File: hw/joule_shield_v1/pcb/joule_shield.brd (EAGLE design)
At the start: 160 x 100 mm, 65 parts, among them U1 BQ25892PWQFN-24, U2 FAN8623WLCSP16, U3 TPS63201PVSON-14, U4 TLV62084PWSON-8, U5 TPS2553PWSON-6, U6 SINGLE-BIT_BUS_TRANSCEIVER, U7 SINGLE-BIT_BUS_TRANSCEIVER

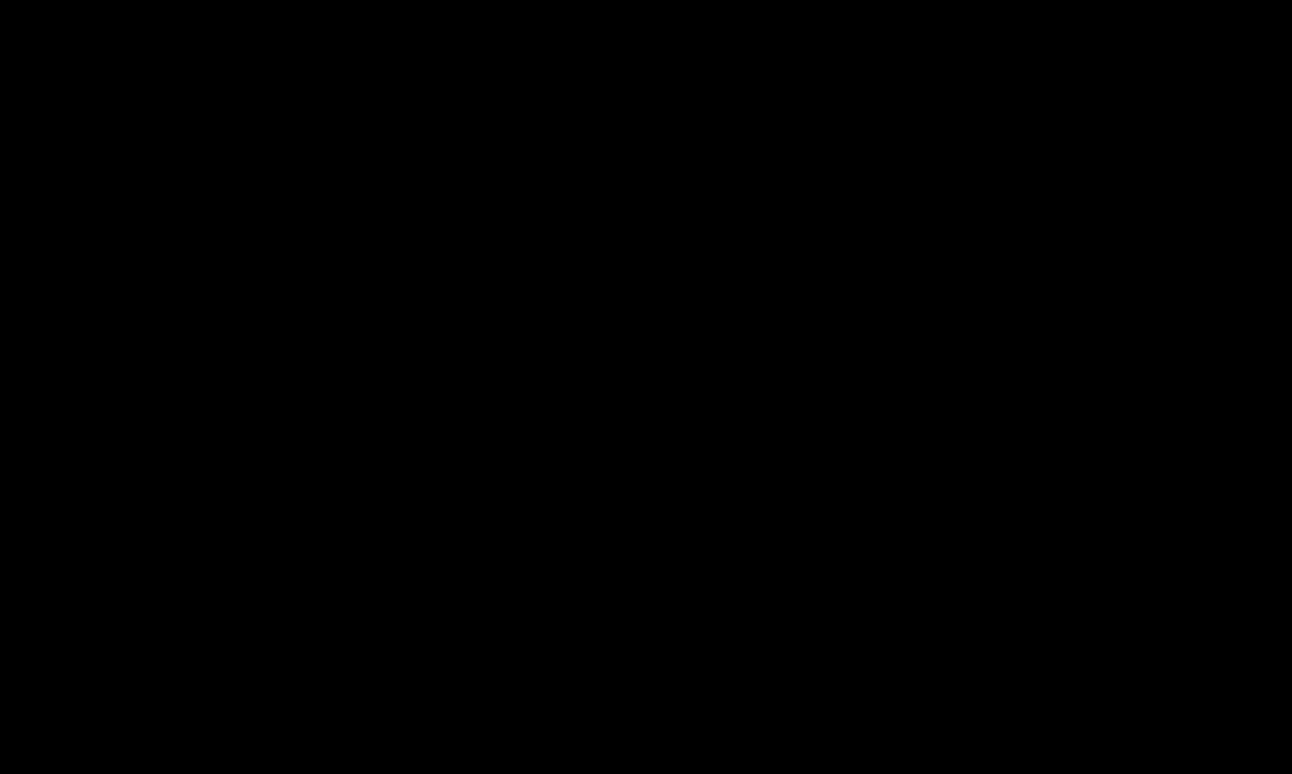
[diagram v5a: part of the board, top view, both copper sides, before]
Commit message: Schematic for servo connectors.
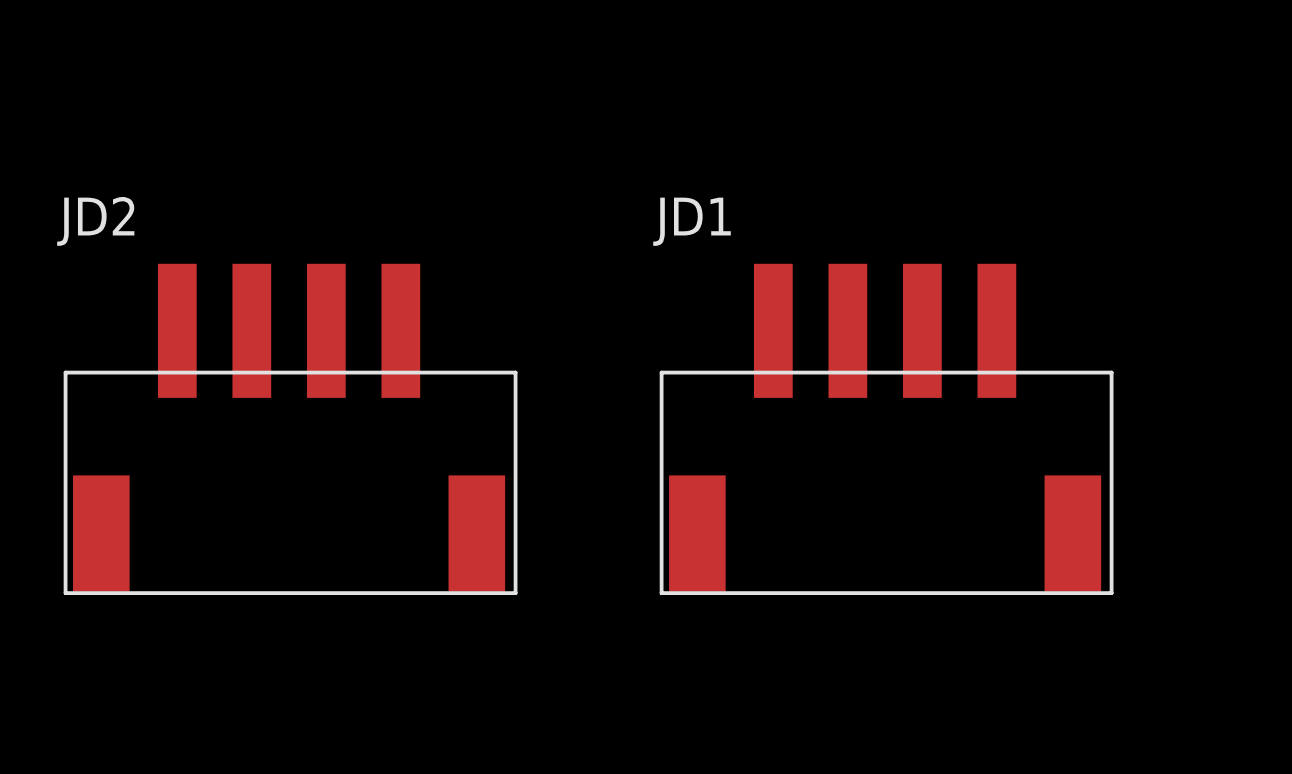
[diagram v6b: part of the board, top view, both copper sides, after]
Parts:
- added JD1, JD2: JST-XH4SMT_RA, joule_shield:JST_XH_SMT_RA_4
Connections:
- net GND: now also JD1.1, JD2.1
- net SERVO_RX_5V: now also JD1.3, JD2.3
- net SERVO_TX_5V: now also JD1.2, JD2.2
- net VIN_CHRG: now also JD1.4, JD2.4
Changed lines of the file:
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@@
 <attribute name="URL" value="" x="-170" y="120" size="1.778" layer="27" display="off"/>
 </element>
+<element name="JD1" library="joule_shield" package="JST_XH_SMT_RA_4" value="JST-XH4SMT_RA" x="-170" y="92"/>
+<element name="JD2" library="joule_shield" package="JST_XH_SMT_RA_4" value="JST-XH4SMT_RA" x="-190" y="92"/>
 </elements>
 <signals>
@@
 <contactref element="U7" pad="2"/>
 <contactref element="C29" pad="P$2"/>
-<wire x1="-167.3" y1="126" x2="-169.25" y2="120" width="0" layer="19" extent="1-1"/>
-<wire x1="-159.3" y1="126" x2="-167.3" y2="126" width="0" layer="19" extent="1-1"/>
-<wire x1="-108.25" y1="71" x2="-159.3" y2="126" width="0" layer="19" extent="1-1"/>
-<wire x1="-108.25" y1="87" x2="-108.25" y2="71" width="0" layer="19" extent="1-1"/>
-<wire x1="-108.25" y1="91" x2="-108.25" y2="87" width="0" layer="19" extent="1-1"/>
-<wire x1="-108.25" y1="95" x2="-108.25" y2="91" width="0" layer="19" extent="1-1"/>
-<wire x1="-108.25" y1="105" x2="-108.25" y2="95" width="0" layer="19" extent="1-1"/>
-<wire x1="-108.25" y1="109" x2="-108.25" y2="105" width="0" layer="19" extent="1-1"/>
-<wire x1="-109" y1="113" x2="-108.25" y2="109" width="0" layer="19" extent="1-1"/>
-<wire x1="-109.95" y1="113.25" x2="-109" y2="113" width="0" layer="19" extent="1-1"/>
-<wire x1="-109.95" y1="112.75" x2="-109.95" y2="113.25" width="0" layer="19" extent="1-1"/>
-<wire x1="-127.95" y1="106" x2="-109.95" y2="112.75" width="0" layer="19" extent="1-1"/>
+<contactref element="JD1" pad="1"/>
+<contactref element="JD2" pad="1"/>
+<wire x1="-135.25" y1="86" x2="-193.75" y2="96.6" width="0" layer="19" extent="1-1"/>
+<wire x1="-128.25" y1="90" x2="-135.25" y2="86" width="0" layer="19" extent="1-1"/>
+<wire x1="-135" y1="96.7" x2="-128.25" y2="90" width="0" layer="19" extent="1-1"/>
+<wire x1="-128.25" y1="102" x2="-135" y2="96.7" width="0" layer="19" extent="1-1"/>
+<wire x1="-127.95" y1="106" x2="-128.25" y2="102" width="0" layer="19" extent="1-1"/>
 <wire x1="-129" y1="106" x2="-127.95" y2="106" width="0" layer="19" extent="1-1"/>
-<wire x1="-128.25" y1="102" x2="-127.95" y2="106" width="0" layer="19" extent="1-1"/>
-<wire x1="-135" y1="96.7" x2="-128.25" y2="102" width="0" layer="19" extent="1-1"/>
-<wire x1="-128.25" y1="90" x2="-135" y2="96.7" width="0" layer="19" extent="1-1"/>
-<wire x1="-135.25" y1="86" x2="-128.25" y2="90" width="0" layer="19" extent="1-1"/>
+<wire x1="-109.95" y1="112.75" x2="-127.95" y2="106" width="0" layer="19" extent="1-1"/>
+<wire x1="-109.95" y1="113.25" x2="-109.95" y2="112.75" width="0" layer="19" extent="1-1"/>
+<wire x1="-109" y1="113" x2="-109.95" y2="112.75" width="0" layer="19" extent="1-1"/>
+<wire x1="-108.25" y1="109" x2="-109" y2="113" width="0" layer="19" extent="1-1"/>
+<wire x1="-108.25" y1="105" x2="-108.25" y2="109" width="0" layer="19" extent="1-1"/>
+<wire x1="-108.25" y1="95" x2="-108.25" y2="105" width="0" layer="19" extent="1-1"/>
+<wire x1="-108.25" y1="91" x2="-108.25" y2="95" width="0" layer="19" extent="1-1"/>
+<wire x1="-108.25" y1="87" x2="-108.25" y2="91" width="0" layer="19" extent="1-1"/>
+<wire x1="-108.25" y1="71" x2="-108.25" y2="87" width="0" layer="19" extent="1-1"/>
 <wire x1="-79.4" y1="110" x2="-108.25" y2="109" width="0" layer="19" extent="1-1"/>
 <wire x1="-78.4" y1="109.8" x2="-79.4" y2="110" width="0" layer="19" extent="1-1"/>
@@
 <wire x1="-14.49" y1="82.55" x2="-18.3" y2="82.55" width="0" layer="19" extent="1-1"/>
 <wire x1="-22.11" y1="86.36" x2="-18.3" y2="82.55" width="0" layer="19" extent="1-1"/>
+<wire x1="-159.3" y1="126" x2="-129" y2="106" width="0" layer="19" extent="1-1"/>
+<wire x1="-167.3" y1="126" x2="-159.3" y2="126" width="0" layer="19" extent="1-1"/>
+<wire x1="-169.25" y1="120" x2="-167.3" y2="126" width="0" layer="19" extent="1-1"/>
+<wire x1="-173.75" y1="96.6" x2="-169.25" y2="120" width="0" layer="19" extent="1-1"/>
 </signal>
 <signal name="N$2">
@@
 <contactref element="C2" pad="P$1"/>
 <contactref element="C3" pad="P$1"/>
-<wire x1="-19.8" y1="74.93" x2="-15.99" y2="74.93" width="0" layer="19" extent="1-1"/>
-<wire x1="-23.61" y1="74.93" x2="-19.8" y2="74.93" width="0" layer="19" extent="1-1"/>
+<contactref element="JD1" pad="4"/>
+<contactref element="JD2" pad="4"/>
+<wire x1="-166.25" y1="96.6" x2="-186.25" y2="96.6" width="0" layer="19" extent="1-1"/>
+<wire x1="-23.61" y1="74.93" x2="-166.25" y2="96.6" width="0" layer="19" extent="1-1"/>
+<wire x1="-19.8" y1="74.93" x2="-23.61" y2="74.93" width="0" layer="19" extent="1-1"/>
+<wire x1="-15.99" y1="74.93" x2="-19.8" y2="74.93" width="0" layer="19" extent="1-1"/>
 <wire x1="-18.485" y1="71.1" x2="-19.8" y2="74.93" width="0" layer="19" extent="1-1"/>
 </signal>
@@
 <signal name="SERVO_TX_5V">
 <contactref element="U6" pad="3"/>
+<contactref element="JD1" pad="2"/>
+<contactref element="JD2" pad="2"/>
+<wire x1="-171.25" y1="96.6" x2="-191.25" y2="96.6" width="0" layer="19" extent="1-1"/>
+<wire x1="-159.3" y1="125.05" x2="-171.25" y2="96.6" width="0" layer="19" extent="1-1"/>
 </signal>
 <signal name="SERVO_RX_5V">
 <contactref element="U7" pad="3"/>
+<contactref element="JD1" pad="3"/>
+<contactref element="JD2" pad="3"/>
+<wire x1="-168.75" y1="96.6" x2="-188.75" y2="96.6" width="0" layer="19" extent="1-1"/>
+<wire x1="-167.3" y1="125.05" x2="-168.75" y2="96.6" width="0" layer="19" extent="1-1"/>
 </signal>
 <signal name="JOULE_RX_18V">

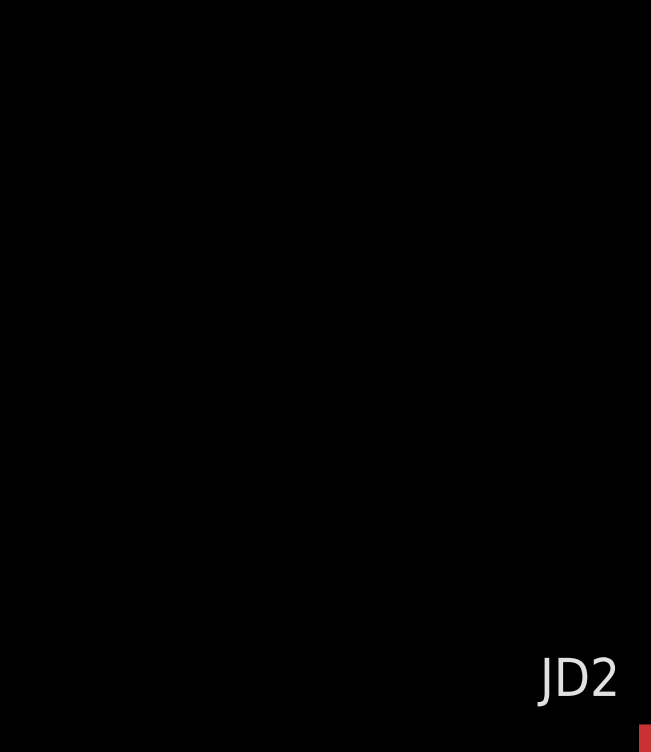
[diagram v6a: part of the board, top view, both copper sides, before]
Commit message: Add input reverse protection and fuse.
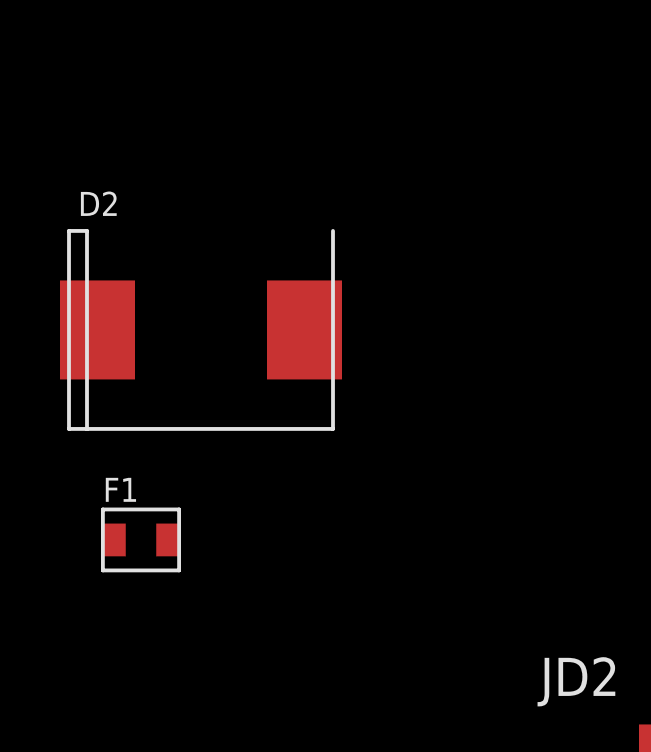
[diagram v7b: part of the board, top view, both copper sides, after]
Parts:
- added D2: (no value), joule_shield:B520C
- added F1: FUSEFUSE_467, joule_shield:FUSE_467
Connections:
- new net N$28: D2.2, JD1.4, JD2.4
- new net N$31: D2.1, F1.1
- net VIN_CHRG: now also F1.2; no longer JD1.4, JD2.4
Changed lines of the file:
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@@
 <element name="JD1" library="joule_shield" package="JST_XH_SMT_RA_4" value="JST-XH4SMT_RA" x="-170" y="92"/>
 <element name="JD2" library="joule_shield" package="JST_XH_SMT_RA_4" value="JST-XH4SMT_RA" x="-190" y="92"/>
+<element name="F1" library="joule_shield" package="FUSE_467" value="FUSEFUSE_467" x="-211" y="105">
+<attribute name="DPN" value="F1400CT-ND" x="-211" y="105" size="1.778" layer="27" display="off"/>
+<attribute name="MF" value="Littlefuse" x="-211" y="105" size="1.778" layer="27" display="off"/>
+<attribute name="MPN" value="046703.5NR" x="-211" y="105" size="1.778" layer="27" display="off"/>
+</element>
+<element name="D2" library="joule_shield" package="B520C" value="" x="-209" y="112">
+<attribute name="DPN" value="B520C-FDICT-ND" x="-209" y="112" size="1.778" layer="27" display="off"/>
+<attribute name="MF" value="Diodes Incorporated" x="-209" y="112" size="1.778" layer="27" display="off"/>
+<attribute name="MPN" value="B520C-13-F" x="-209" y="112" size="1.778" layer="27" display="off"/>
+</element>
 </elements>
 <signals>
@@
 <contactref element="C2" pad="P$1"/>
 <contactref element="C3" pad="P$1"/>
-<contactref element="JD1" pad="4"/>
-<contactref element="JD2" pad="4"/>
-<wire x1="-166.25" y1="96.6" x2="-186.25" y2="96.6" width="0" layer="19" extent="1-1"/>
-<wire x1="-23.61" y1="74.93" x2="-166.25" y2="96.6" width="0" layer="19" extent="1-1"/>
+<contactref element="F1" pad="2"/>
+<wire x1="-23.61" y1="74.93" x2="-210.111" y2="105" width="0" layer="19" extent="1-1"/>
 <wire x1="-19.8" y1="74.93" x2="-23.61" y2="74.93" width="0" layer="19" extent="1-1"/>
 <wire x1="-15.99" y1="74.93" x2="-19.8" y2="74.93" width="0" layer="19" extent="1-1"/>
@@
 <contactref element="U7" pad="4"/>
 </signal>
+<signal name="N$28">
+<contactref element="JD1" pad="4"/>
+<contactref element="JD2" pad="4"/>
+<contactref element="D2" pad="2"/>
+<wire x1="-186.25" y1="96.6" x2="-205.55" y2="112" width="0" layer="19" extent="1-1"/>
+<wire x1="-166.25" y1="96.6" x2="-186.25" y2="96.6" width="0" layer="19" extent="1-1"/>
+</signal>
+<signal name="N$31">
+<contactref element="D2" pad="1"/>
+<contactref element="F1" pad="1"/>
+<wire x1="-211.889" y1="105" x2="-212.45" y2="112" width="0" layer="19" extent="1-1"/>
+</signal>
 </signals>

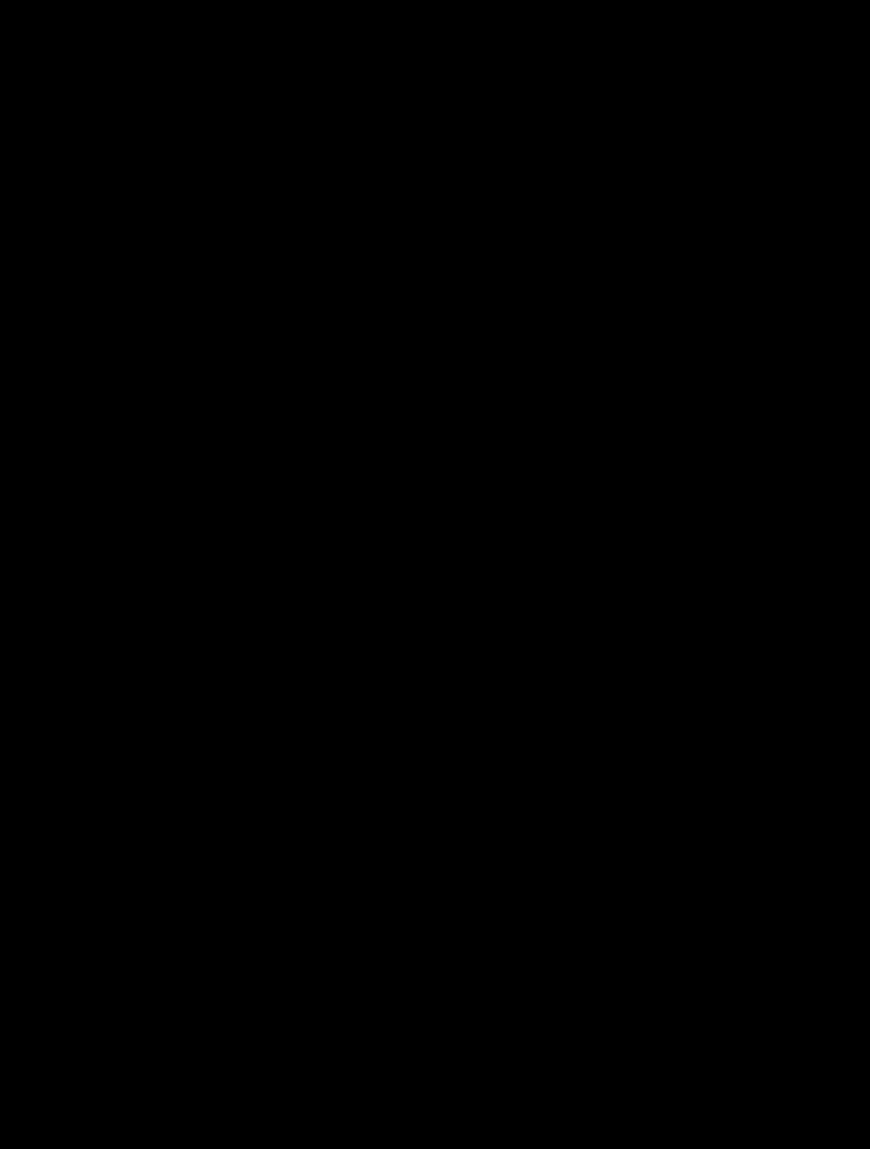
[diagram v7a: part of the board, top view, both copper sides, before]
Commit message: Schematic for USB and Joule connectors.
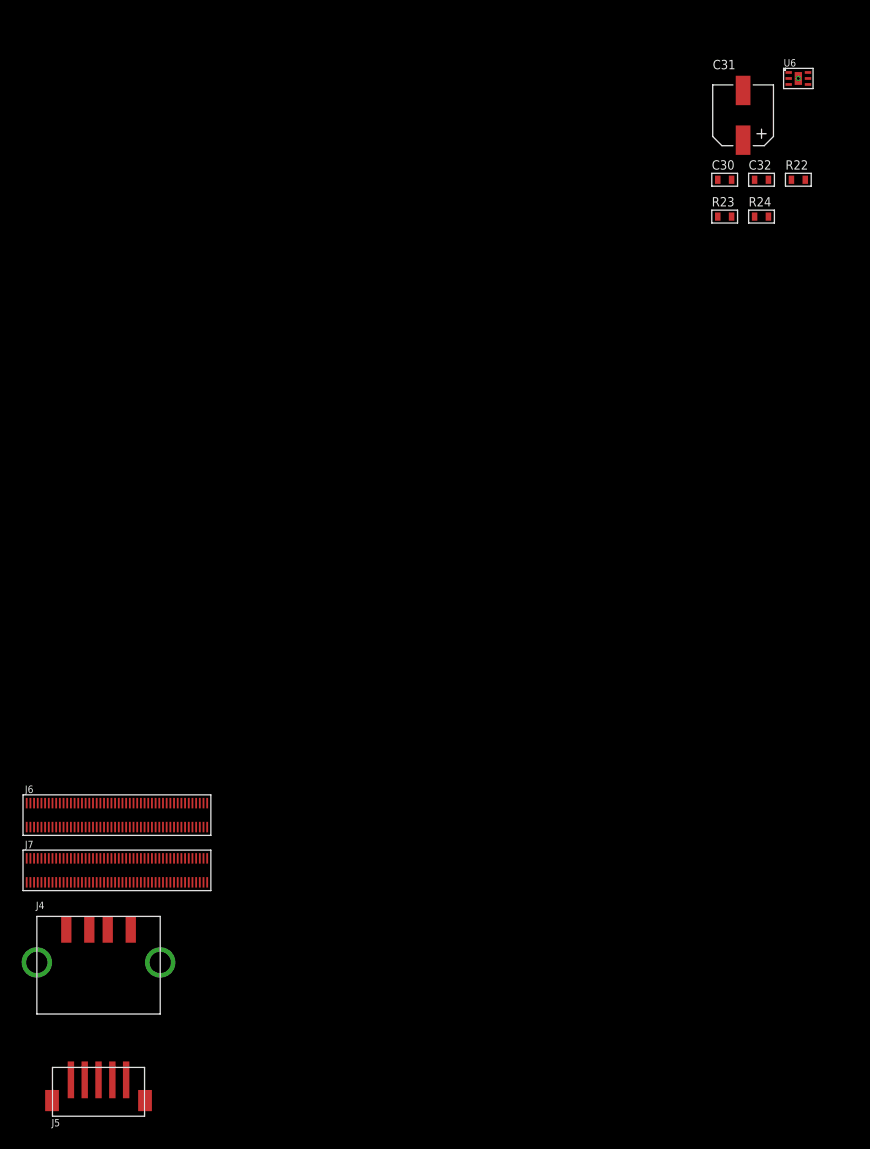
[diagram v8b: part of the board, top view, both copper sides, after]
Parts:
- added C30: 10uF, mf_passives:C0603
- added C31: 100uF, mf_passives:CP6.3MM
- added C32: 0.1uF, mf_passives:C0603
- added J4: USB_AUSB_A_SMT_RA, joule_shield:USB_RECPT_87583
- added J5: JST-ZH5JST_ZH_SMT_VERT, joule_shield:JST_ZH_SMT_VERT_5
- added J6: INTEL_JOULE_J6, joule_shield:HIROSE-40C-100DS
- added J7: INTEL_JOULE_J7, joule_shield:HIROSE-40C-100DS
- added R22, R23: 100k, mf_passives:R0603
- added R24: 15k, mf_passives:R0603
- added U8: SINGLE-BIT_BUS_TRANSCEIVER, joule_shield:SOT23-6
- U6: value SINGLE-BIT_BUS_TRANSCEIVER -> TPS2553PWSON-6; device joule_shield:SOT23-6 -> joule_shield:PWSON-6
- moved U6 57.8 mm to (-129.0, 76.0)
- moved U7 8.00 mm to (-158.0, 126.0)
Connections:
- new net N$32: R22.P$2, U6.3
- new net N$33: R23.P$2, U6.4
- new net N$34: R24.P$1, U6.2
- new net USB2_0_N: J4.2, J6.8
- new net USB2_0_P: J4.3, J6.6
- new net USB2_1_N: J5.2, J7.63
- new net USB2_1_P: J5.3, J7.65
- new net V5P0V_USBB: C31.P$1, C32.P$1, J5.1, U6.1
- net GND: now also C30.P$2, C31.P$2, C32.P$2, J4.4, J4.S1, J4.S2, J5.4, J5.5, J6.10, J6.100, J6.19, J6.4, J6.42, J6.48, J6.54, J6.60, J6.66, J6.72, J6.73, J6.82, J6.86, J6.96, J6.98, J7.10, J7.16, J7.17, J7.2, J7.23, J7.24, J7.29, J7.30, J7.35, J7.36, J7.41, J7.42, J7.5, J7.54, J7.60, J7.61, J7.67, J7.74, J7.8, J7.80, J7.84, J7.85, J7.90, J7.91, J7.93, J7.96, J7.99, R24.P$2, U6.5, U6.G0, U6.G1, U8.2; no longer U6.2
- net JOULE_RX_18V: now also U7.4; no longer U6.4
- net JOULE_TX_18V: now also U8.4; no longer U7.4
- net SERVO_RX_5V: now also U8.3; no longer U7.3
- net SERVO_TX_5V: now also U7.3; no longer U6.3
- net V1P8V: now also U7.6, U8.1, U8.5; no longer U6.6, U7.1, U7.5
- net V5P0V: now also C30.P$1, R22.P$1, R23.P$1, U6.6, U7.1, U7.5, U8.6; no longer U6.1, U6.5, U7.6
- net V5P0V_USBA: now also J4.1
- net VDD1: now also J6.36
- net VDD3: now also J6.30
- net VIN_CHRG: now also J6.37
- net VSYS: now also J6.12, J6.15, J6.17, J6.2, J6.5, J6.7, J7.1, J7.20, J7.22, J7.3, J7.32, J7.34
